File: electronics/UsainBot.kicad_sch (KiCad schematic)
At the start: 0 parts

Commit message: Dessine le schéma complet de la carte sur sept feuilles hiérarchiques
Le projet KiCad ne portait qu'une feuille vide. Il contient maintenant les
252 composants de la carte, répartis par fonction : alimentation et charge
USB-C, microcontrôleur, ponts en H, barrette de ligne, capteurs, IHM,
traces et turbine. Les feuilles communiquent par étiquettes globales
plutôt que par entrées de feuille : un bloc se lit seul, et renommer un
signal ne demande pas de retoucher la racine. ERC à zéro erreur et zéro
avertissement, avec le contrôle des étiquettes globales orphelines activé.

Vérifie le brochage du §6 broche à broche contre le symbole
STM32H723VGTx : les douze voies de la barrette tombent bien sur ADC1 et
ADC2, la surveillance sur les seules broches ADC3 du boîtier. Le fichier
CubeMX, lui, est resté sur l'ancien G431 en LQFP32 et n'a pas servi.

Tire les câblages du DRV8874 et du BQ25887 de leurs fiches techniques
plutôt que d'un résumé. Le brochage HTSSOP-16 qui circule omet les entrées
de commande ; le vrai place EN/IN1 en 1 et PMODE en 16. Le chargeur suit
la figure 69 de la SLUSD89B : inductance de 1 µH, 44 µF sur PMID et SNS,
diviseur TS 5,23 k / 30,1 k.

Ajoute neuf symboles dans kicad-lib/Pacabot.kicad_sym, faute d'équivalent
KiCad ou pour retyper des broches que l'ERC refusait — le DRV8874 en
HTSSOP-16, l'AO4407A en SO-8 dont les huit pattes ne rentrent pas dans un
Q_PMOS à trois broches, et les phototransistors de l'ITR8307 passés en
passif. Provenance et réserves dans le README de la bibliothèque.

Génère le tout par electronics/tools/, qui refuse de terminer sur un
recouvrement de fils, une extrémité tombée au milieu d'un fil étranger, un
texte écrit par-dessus un boîtier ou un composant posé dans le cartouche.
Ce dernier contrôle a fait ressortir deux diodes montées à l'envers : le
témoin de charge, en inverse sur un collecteur ouvert, et la roue libre du
buzzer, qui court-circuitait la bobine au lieu d'écrêter sa surtension.
Relancer ces scripts écrase tout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
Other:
- added sheet Alimentation (01-power.kicad_sch)
- added sheet Barrette (04-line-array.kicad_sch)
- added sheet Capteurs (05-sensors.kicad_sch)
- added sheet IHM (06-hmi.kicad_sch)
- added sheet MCU (02-mcu.kicad_sch)
- added sheet Moteurs (03-motors.kicad_sch)
- added sheet Traces et turbine (07-comms.kicad_sch)
- note added: "Deux DRV8874 en mode PWM, limitation de courant, connecteurs moteur + encodeur, filtrage de quadrature"
- note added: "Deux VL53L1X sur languette sechable, voie analogique rapide a gauche, LSM6DSO sur SPI2"
- note added: "Douze ITR8307 au pas de 10 mm, deux bancs d emetteurs pulses, charges d emetteur sur le rail analogique"
- note added: "Flash W25Q128 sur SPI3, module BLE a alimentation commutee, embase ESC et puissance de turbine"
- note added: "Les feuilles communiquent par etiquettes globales : chaque bloc se lit seul, et le renommage d un signal se propage sans retoucher les entrees de feuille."
- note added: "OLED I2C2, switch 5 directions, buzzer sur TIM17, bouton et jack de depart, temoins"
- note added: "Points ouverts reportes du document d architecture : - interrupteur et fusible dimensionnes a 10 A ; si la turbine tire vraiment 15 A, c est toute la chaine de coupure qu il faut remonter, pas seulement le fusible ; - OPV302 et BPW77 probablement hors bibliotheque JLCPCB : pose manuelle ou repli ToF ; - valeurs marquees a recaler : R116 (frequence du buck), R107 (courant d equilibrage), charge du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"
- note added: "STM32H723VGT6 en LQFP100, decouplage, quartz 25 MHz, reset, BOOT0, empreinte Tag-Connect SWD + SWO"
- note added: "USB-C, chargeur elevateur BQ25887, pack 2S, coupure generale, anti-inversion, buck 3,3 V, rail 3V3A"
- note added: "UsainBot - architecture materielle"
- company: (none) -> Pacabot
- title: (none) -> UsainBot - robot suiveur de ligne, epreuve Formule 1 TNRS

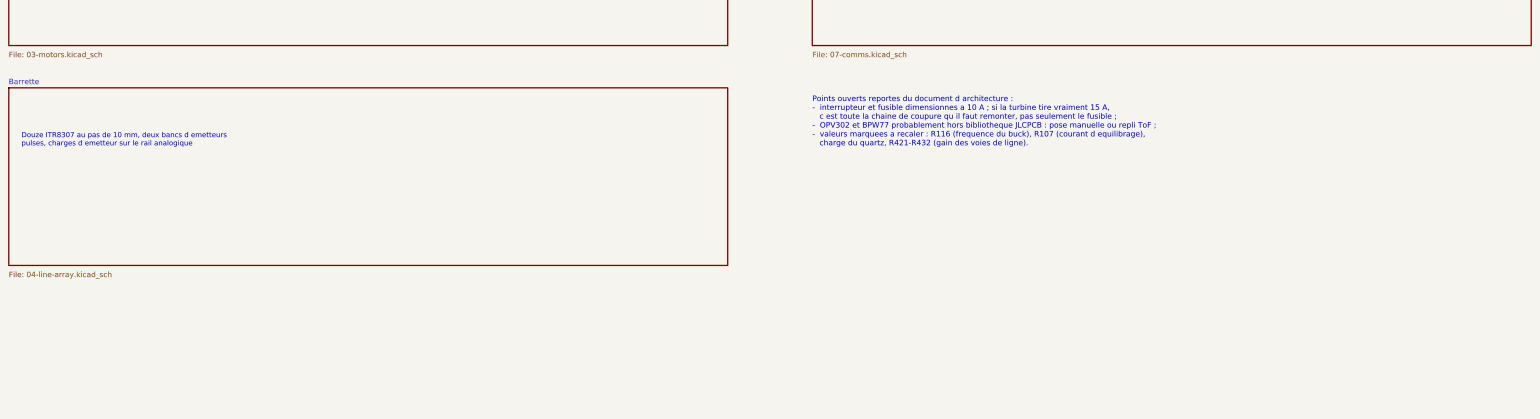
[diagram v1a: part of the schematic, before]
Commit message: Passe le microcontrôleur en LQFP144 et lit les deux courants au même instant
Le LQFP100 avait ses seize entrées ADC prises — douze voies de ligne, trois
de télémétrie, une sortie de multiplexeur — et c'est ce multiplexeur qui
posait le vrai problème : il interdisait par construction de lire les deux
courants moteur ensemble. On lisait un moteur, on commutait, on attendait
l'établissement, on lisait l'autre. Le STM32H723ZGT6 en LQFP144 place
PF11 sur ADC1_INP2 et PF13 sur ADC2_INP2 : même numéro de voie sur deux
convertisseurs, donc une lecture simultanée en mode double, et le 74HC4051
disparaît de la carte.

Le brochage étant donné par nom de port et non par numéro de broche, le
passage a coûté deux affectations sur quatre-vingt-sept. Une affectation est
un choix de port — PA0 porte la voie de ligne 00 — jamais un choix de patte.
Une table numérotée aurait demandé de recopier 144 lignes à la main, et une
erreur de brochage ne se voit pas à l'ERC.

Ajoute une huitième feuille, les témoins de ligne. Ce qu'on regarde pendant
un essai n'est pas un témoin d'état générique, c'est ce que voit la
moustache : une LED par capteur, à l'aplomb du capteur qu'elle rapporte, et
un capteur borgne se voit avant la course plutôt qu'après. Le rapport
cyclique suit le signal, sinon rien ne dirait si la ligne est au bord ou au
centre du trait. PCA9685 à l'adresse 0x40 sur I²C2, 52 octets par rafale
soit 1,2 ms à 400 kHz, en DMA hors de la boucle rapide.

Remplace l'interrupteur à glissière par une mise sous tension à bouton
poussoir : une impulsion amorce, le microcontrôleur se tient lui-même, et
c'est lui qui coupe. La glissière demandait une place au bord de carte que
le pack, l'équilibrage et les fils de l'ESC ont fini par prendre — et elle
ne savait pas éteindre proprement, couper le 3,3 V sous les pieds du
firmware n'ayant jamais rien écrit dans la flash.

Ajoute au générateur le contrôle qui manquait : deux extrémités de nets
différents au même point. Il a fallu qu'il relie B+ à B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
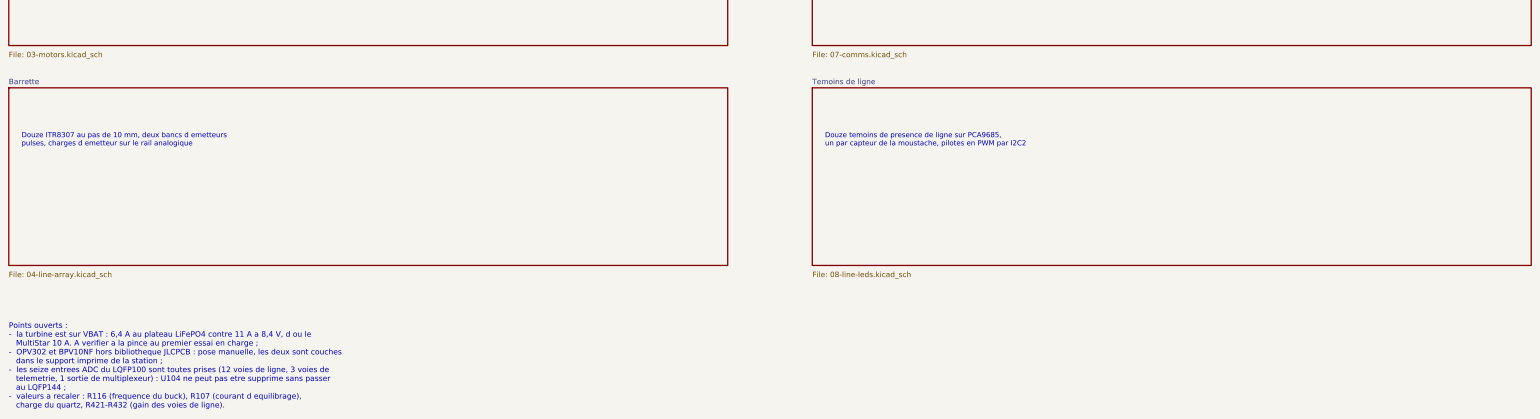
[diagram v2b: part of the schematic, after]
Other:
- added sheet Temoins de ligne (08-line-leds.kicad_sch)
- note added: "Douze temoins de presence de ligne sur PCA9685, un par capteur de la moustache, pilotes en PWM par I2C2"
- note added: "Points ouverts : - la turbine est sur VBAT : 6,4 A au plateau LiFePO4 contre 11 A a 8,4 V, d ou le MultiStar 10 A. A verifier a la pince au premier essai en charge ; - OPV302 et BPV10NF hors bibliotheque JLCPCB : pose manuelle, les deux sont couches dans le support imprime de la station ; - les seize entrees ADC du LQFP100 sont toutes prises (12 voies de ligne, 3 voies de telemetrie, 1 sortie de 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"
- note removed: "Points ouverts reportes du document d architecture : - interrupteur et fusible dimensionnes a 10 A ; si la turbine tire vraiment 15 A, c est toute la chaine de coupure qu il faut remonter, pas seulement le fusible ; - OPV302 et BPW77 probablement hors bibliotheque JLCPCB : pose manuelle ou repli ToF ; - valeurs marquees a recaler : R116 (frequence du buck), R107 (courant d equilibrage), charge du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"
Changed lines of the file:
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@@
+		)
+	)
+	(sheet
+		(at 210 212)
+		(size 170 42)
+		(exclude_from_sim no)
+		(in_bom yes)
+		(on_board yes)
+		(dnp no)
+		(fields_autoplaced yes)
+		(stroke
+			(width 0.1524)
+			(type solid)
+		)
+		(fill
+			(color 0 0 0 0.0000)
+		)
+		(property "Sheetname" "Temoins de ligne"
+			(at 210 211.2888 0)
+			(effects
+				(font
+					(size 1.27 1.27)
+				)
+				(justify left bottom)
+			)
+		)
+		(property "Sheetfile" "08-line-leds.kicad_sch"
+			(at 210 255.4224 0)
+			(effects
+				(font
+					(size 1.27 1.27)
+				)
+				(justify left top)
+			)
+		)
+		(instances
+			(project "UsainBot"
+				(path "/e216f09c-2662-6258-2b51-4f4f498f79d0"
+					(page "9")
+				)
+			)
 		)
 	)
@@
 		)
 	)
-	(text "Points ouverts reportes du document d architecture :\n-  interrupteur et fusible dimensionnes a 10 A ; si la turbine tire vraiment 15 A,\n   c est toute la chaine de coupure qu il faut remonter, pas seulement le fusible ;\n-  OPV302 et BPW77 probablement hors bibliotheque JLCPCB : pose manuelle ou repli ToF ;\n-  valeurs marquees a recaler : R116 (frequence du buck), R107 (courant d equilibrage),\n   charge du quartz, R421-R432 (gain des voies de ligne)."
+	(text "Douze temoins de presence de ligne sur PCA9685,\nun par capteur de la moustache, pilotes en PWM par I2C2"
 		(exclude_from_sim no)
-		(at 210 226 0)
+		(at 213 226 0)
+		(effects
+			(font
+				(size 1.2 1.2)
+			)
+			(justify left bottom)
+		)
+	)
+	(text "Points ouverts :\n-  la turbine est sur VBAT : 6,4 A au plateau LiFePO4 contre 11 A a 8,4 V, d ou le\n   MultiStar 10 A. A verifier a la pince au premier essai en charge ;\n-  OPV302 et BPV10NF hors bibliotheque JLCPCB : pose manuelle, les deux sont couches\n   dans le support imprime de la station ;\n-  les seize entrees ADC du LQFP100 sont toutes prises (12 voies de ligne, 3 voies de\n   telemetrie, 1 sortie de multiplexeur) : U104 ne peut pas etre supprime sans passer\n   au LQFP144 ;\n-  valeurs a recaler : R116 (frequence du buck), R107 (courant d equilibrage),\n   charge du quartz, R421-R432 (gain des voies de ligne)."
+		(exclude_from_sim no)
+		(at 20 288 0)
 		(effects
 			(font
@@
 			(page "8")
 		)
+		(path "/ba1ecbcf-1c65-895e-8b85-2425aaf9186b"
+			(page "9")
+		)
 	)

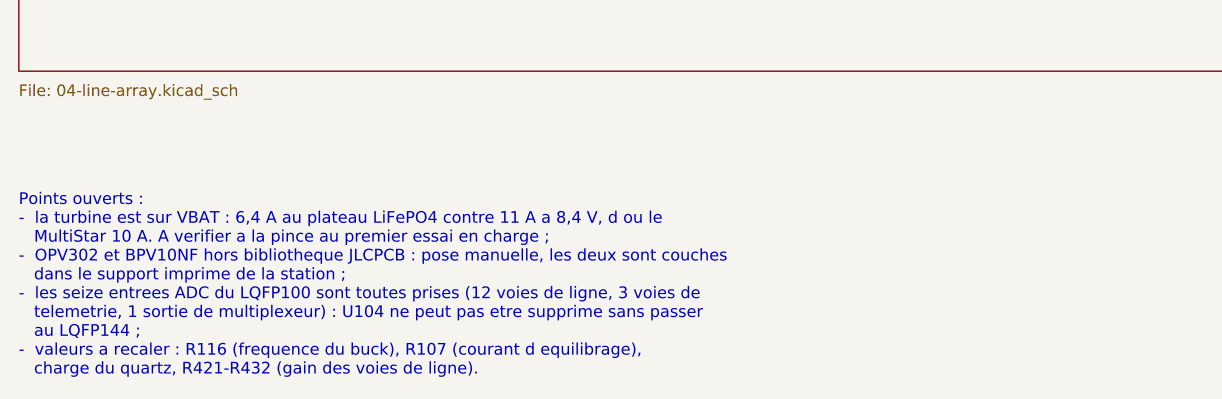
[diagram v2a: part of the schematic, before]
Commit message: Replace la carte autour de ses chaînes analogiques et y intègre le pack commun et l'ESC
Le placement du 4 septembre rangeait les pièces par zone. Celui-ci part des
nets et des vraies pastilles, et affecte chaque condensateur à une broche
plutôt qu'à une couronne autour du boîtier. Le STM32 pivote de 180° sur son
centre pour tourner son côté analogique vers la barrette. Chaque station
laser reçoit son propre TLV9064 (U504 s'ajoute pour la station L), et la
liaison photodiode → TIA tombe de 34, 56 et 69 mm à 3,1, 7,4 et 2,9 mm. La
boucle de retour du TIA passe de 140–150 mm à 3,55. Cinq découplages
suivent : C568, C569/C570 sur VREF_RX, C223/C224 sur VBAT du MCU et C351
sur VREF_MOT du pont droit.

`layout.py`, `layout_fit.json` et `place_pcb.py --reset` ne décrivent plus
cette carte. Le README le dit en tête, et les nouveaux outils partent du
PCB courant, jamais de l'ancienne table. `audit_placement_geometry.py` relit
les courtyards orientés et les contrôle sous Shapely, `placement_metrics.py`
et `preview_analog_paths.py` mesurent distances et couloirs sans poser une
piste. `refine_placement.py` calcule la table, `apply_refined_placement.py`
l'écrit en vérifiant verrous et UUID : il ne se rejoue pas après une
retouche à la main.

L'alimentation change de nature. Le pack LiFePO4 et son ESC sur VBAT
laissent place à un pack 2S commun, chimie encore à choisir, que la carte,
les moteurs et la turbine partagent. Une seule prise MR30 à trois contacts
porte GND, point milieu et VPACK, et remplace XT30 + JST-XH. L'ESC devient
un EMAX Bullet 12A (12 A continu, 15 A crête, sans BEC) sur VPACK brut,
monté debout sur J103. J104 et J702 disparaissent. ESC103 et M703 sont des
symboles hors carte : les phases moteur ne reçoivent aucun pad fictif, et
le module ne compte qu'une fois dans la nomenclature. R107 passe de 10 à
47 Ω pour ramener l'équilibrage à 88 mA et 0,36 W, sous le watt de son
boîtier 2512. La recharge reste inhibée par défaut matériel tant que
cellules, profil et fir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
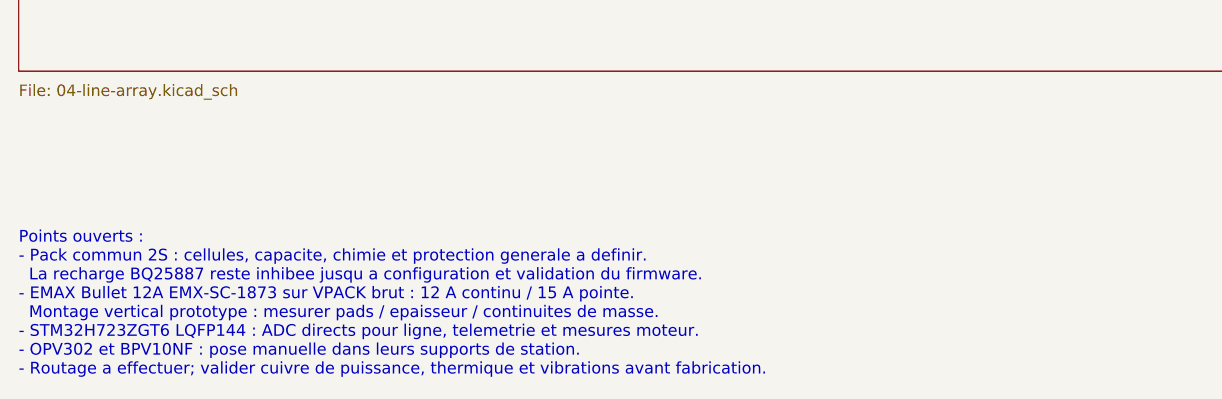
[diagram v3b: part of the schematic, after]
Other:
- note added: "Points ouverts : - Pack commun 2S : cellules, capacite, chimie et protection generale a definir. La recharge BQ25887 reste inhibee jusqu a configuration et validation du firmware. - EMAX Bullet 12A EMX-SC-1873 sur VPACK brut : 12 A continu / 15 A pointe. Montage vertical prototype : mesurer pads / epaisseur / continuites de masse. - STM32H723ZGT6 LQFP144 : ADC directs pour ligne, telemetrie et me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"
- note removed: "Points ouverts : - la turbine est sur VBAT : 6,4 A au plateau LiFePO4 contre 11 A a 8,4 V, d ou le MultiStar 10 A. A verifier a la pince au premier essai en charge ; - OPV302 et BPV10NF hors bibliotheque JLCPCB : pose manuelle, les deux sont couches dans le support imprime de la station ; - les seize entrees ADC du LQFP100 sont toutes prises (12 voies de ligne, 3 voies de telemetrie, 1 sortie de 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"
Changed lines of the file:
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@@
 		(rev "A")
 		(company "Pacabot")
-		(comment 1 "STM32H723VGT6 - 12 voies de ligne - 2 ponts DRV8874 - pack 2S LiFePO4")
+		(comment 1 "STM32H723ZGT6 - 12 voies de ligne - 2 ponts DRV8874 - pack 2S - chimie a definir")
 		(comment 2 "Reglement Formule 1 v2.11 (2025) - carte 4 couches, assemblage JLCPCB")
 	)
@@
 		)
 	)
-	(text "Points ouverts :\n-  la turbine est sur VBAT : 6,4 A au plateau LiFePO4 contre 11 A a 8,4 V, d ou le\n   MultiStar 10 A. A verifier a la pince au premier essai en charge ;\n-  OPV302 et BPV10NF hors bibliotheque JLCPCB : pose manuelle, les deux sont couches\n   dans le support imprime de la station ;\n-  les seize entrees ADC du LQFP100 sont toutes prises (12 voies de ligne, 3 voies de\n   telemetrie, 1 sortie de multiplexeur) : U104 ne peut pas etre supprime sans passer\n   au LQFP144 ;\n-  valeurs a recaler : R116 (frequence du buck), R107 (courant d equilibrage),\n   charge du quartz, R421-R432 (gain des voies de ligne)."
+	(text "Points ouverts :\n- Pack commun 2S : cellules, capacite, chimie et protection generale a definir.\n  La recharge BQ25887 reste inhibee jusqu a configuration et validation du firmware.\n- EMAX Bullet 12A EMX-SC-1873 sur VPACK brut : 12 A continu / 15 A pointe.\n  Montage vertical prototype : mesurer pads / epaisseur / continuites de masse.\n- STM32H723ZGT6 LQFP144 : ADC directs pour ligne, telemetrie et mesures moteur.\n- OPV302 et BPV10NF : pose manuelle dans leurs supports de station.\n- Routage a effectuer; valider cuivre de puissance, thermique et vibrations avant fabrication."
 		(exclude_from_sim no)
 		(at 20 288 0)
